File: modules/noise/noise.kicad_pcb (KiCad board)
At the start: 2 copper layers, 30.5 x 68.6 mm, 4 parts

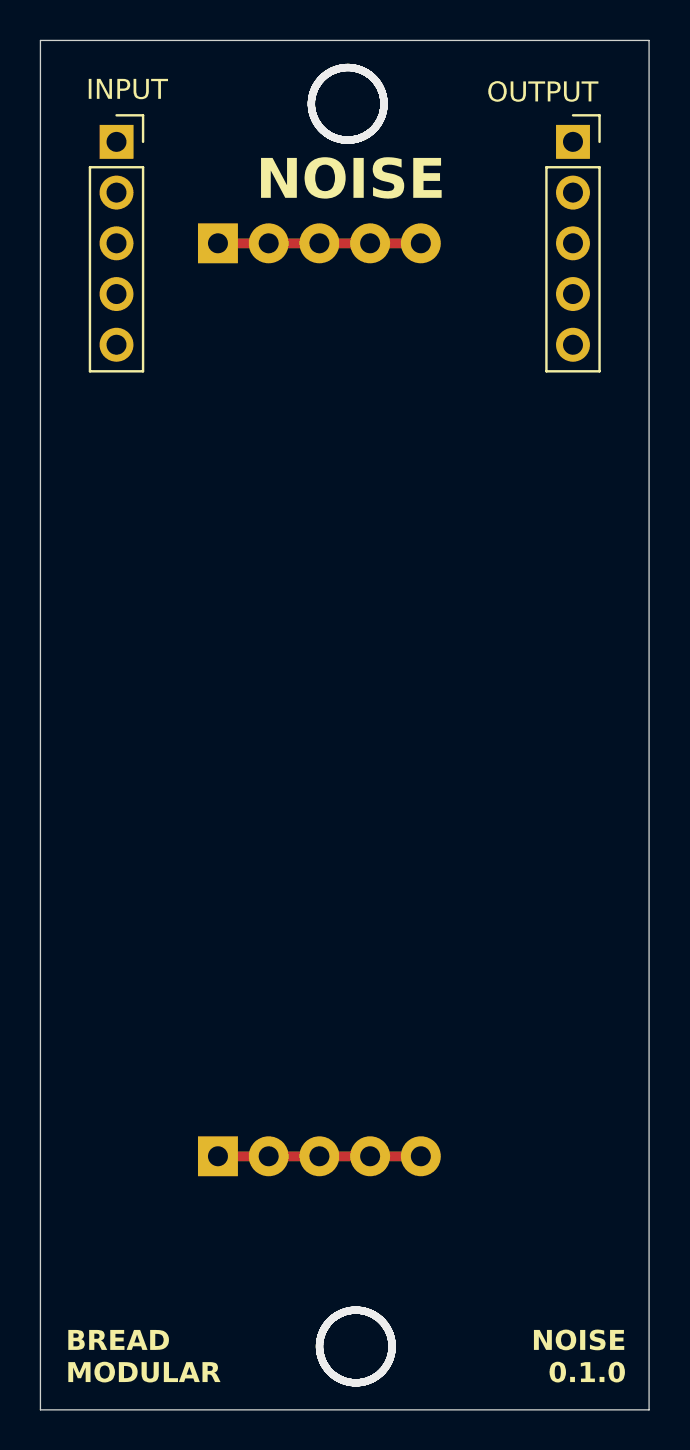
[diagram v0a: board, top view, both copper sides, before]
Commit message: Implement the PCB routing
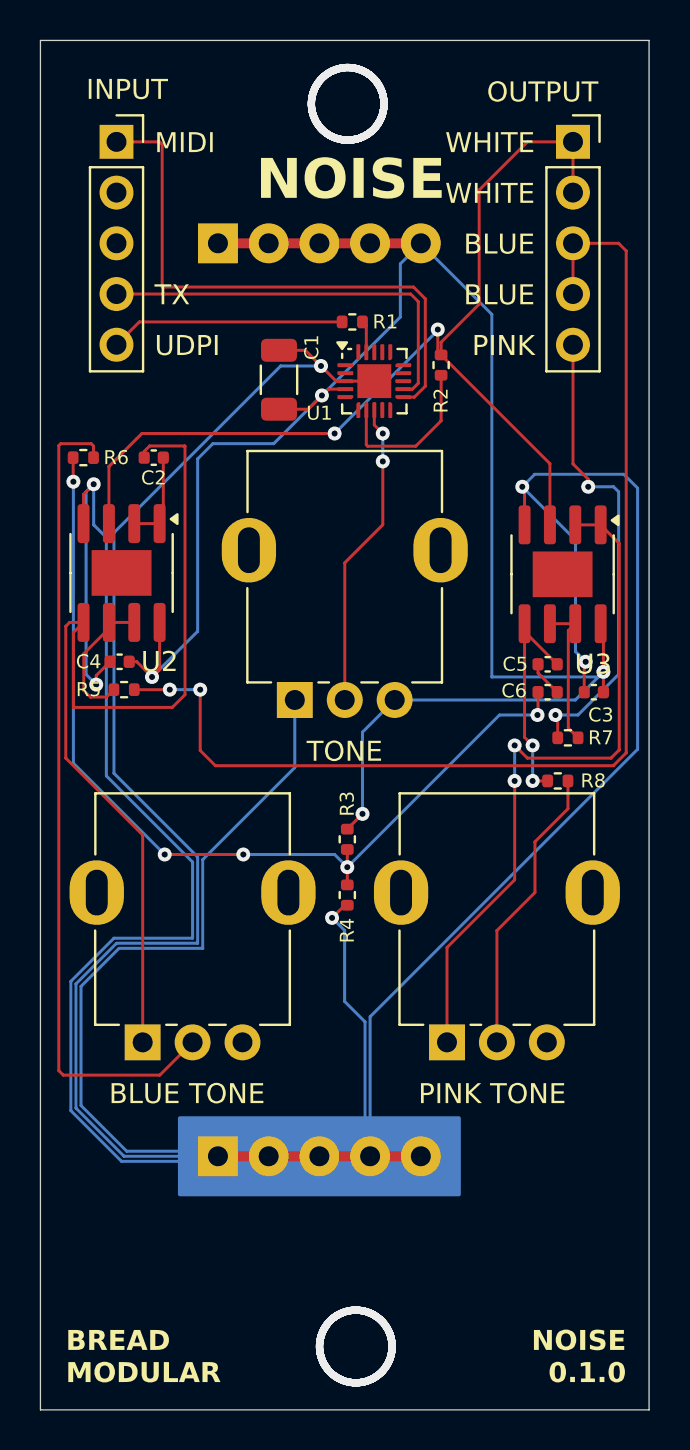
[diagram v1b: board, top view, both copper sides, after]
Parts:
- added C1: 100uf, Capacitor_SMD:C_1206_3216Metric, F.Cu at (58.9, 57.6)
- added C2: 100pf, Capacitor_SMD:C_0402_1005Metric, F.Cu at (52.7, 61.5)
- added C3: 100nf, Capacitor_SMD:C_0402_1005Metric, F.Cu at (74.7, 73.3)
- added C4: 100nf, Capacitor_SMD:C_0402_1005Metric, F.Cu at (51.0, 71.8)
- added C5: 10nf, Capacitor_SMD:C_0402_1005Metric, F.Cu at (72.4, 71.9)
- added C6: 10nf, Capacitor_SMD:C_0402_1005Metric, F.Cu at (72.4, 73.3)
- added R1: 4.7k, Resistor_SMD:R_0402_1005Metric, F.Cu at (62.6, 54.7)
- added R2: 1k, Resistor_SMD:R_0402_1005Metric, F.Cu at (67.1, 56.9)
- added R3: 1k, Resistor_SMD:R_0402_1005Metric, F.Cu at (62.4, 80.6)
- added R4: 1k, Resistor_SMD:R_0402_1005Metric, F.Cu at (62.4, 83.4)
- added R5: 1k, Resistor_SMD:R_0402_1005Metric, F.Cu at (51.2, 73.2)
- added R6: 330, Resistor_SMD:R_0402_1005Metric, F.Cu at (49.1, 61.5)
- added R7: 1k, Resistor_SMD:R_0402_1005Metric, F.Cu at (73.4, 75.6)
- added R8: 22k, Resistor_SMD:R_0402_1005Metric, F.Cu at (72.9, 77.7)
- added RV1: 50k, BreadModular_Pots:Potentiometer_RV09, F.Cu at (59.7, 73.7)
- added RV2: 1M, BreadModular_Pots:Potentiometer_RV09, F.Cu at (52.1, 90.8)
- added RV3: 1M, BreadModular_Pots:Potentiometer_RV09, F.Cu at (67.3, 90.8)
- added U1: ATtiny1616-M, Package_DFN_QFN:VQFN-20-1EP_3x3mm_P0.4mm_EP1.7x1.7mm, F.Cu at (63.7, 57.7)
- added U2: MCP6002-xSN, Package_SO:SOIC-8-1EP_3.9x4.9mm_P1.27mm_EP2.29x3mm, F.Cu at (51.1, 67.3)
- added U3: MCP6002-xSN, Package_SO:SOIC-8-1EP_3.9x4.9mm_P1.27mm_EP2.29x3mm, F.Cu at (73.1, 67.4)
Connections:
- INPUT1 pad 1: unconnected-(INPUT1-Pin_1-Pad1) -> MIDI
- INPUT1 pad 4: unconnected-(INPUT1-Pin_4-Pad4) -> TX
- INPUT1 pad 5: unconnected-(INPUT1-Pin_5-Pad5) -> UDPI
- OUTPUT1 pad 1: unconnected-(OUTPUT1-Pin_1-Pad1) -> WHITE_NOISE
- OUTPUT1 pad 2: unconnected-(OUTPUT1-Pin_2-Pad2) -> WHITE_NOISE
- OUTPUT1 pad 3: unconnected-(OUTPUT1-Pin_3-Pad3) -> BLUE_NOISE
- OUTPUT1 pad 4: unconnected-(OUTPUT1-Pin_4-Pad4) -> BLUE_NOISE
- OUTPUT1 pad 5: unconnected-(OUTPUT1-Pin_5-Pad5) -> PINK_NOISE
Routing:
- net GND: track 10.2 -> 243.7 mm, vias 0 -> 6
- net V_SUPPLY: track 10.2 -> 98.2 mm, vias 0 -> 4
- net BLUE_NOISE: track 0.00 -> 58.5 mm, vias 0 -> 2
- net WHITE_NOISE: track 0.00 -> 51.6 mm, vias 0 -> 2
- net Net-(U2B-+): track 0.00 -> 48.6 mm
- net V_MID: track 0.00 -> 46.8 mm, vias 0 -> 5
- net Net-(R6-Pad1): track 0.00 -> 41.2 mm
- net Net-(U3A--): track 0.00 -> 34.9 mm, vias 0 -> 2
- net MIDI: track 0.00 -> 28.6 mm
- net PINK_NOISE: track 0.00 -> 23.4 mm, vias 0 -> 2
- net TX: track 0.00 -> 20.2 mm
- net Net-(U1-PA7): track 0.00 -> 15.5 mm, vias 0 -> 2
- net Net-(R8-Pad1): track 0.00 -> 14.6 mm
- net UDPI: track 0.00 -> 11.8 mm
- net Net-(U3B-+): track 0.00 -> 11.5 mm, vias 0 -> 2
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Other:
- board text added: "BLUE"
- board text added: "BLUE TONE"
- board text added: "MIDI"
- board text added: "PINK"
- board text added: "PINK TONE"
- board text added: "TONE"
- board text added: "TX"
- board text added: "UDPI"
- board text added: "WHITE"
